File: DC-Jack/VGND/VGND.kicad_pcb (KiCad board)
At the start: 4 copper layers, 32 x 83 mm, 22 parts, among them J1 AudioJack2_Ground, J2 AudioJack2_Ground, J3 Barrel_Jack_Switch, J4 Conn_02x04_Odd_Even, J5 Conn_02x04_Odd_Even, U1 OPA1655, U2 TLE2426xLP

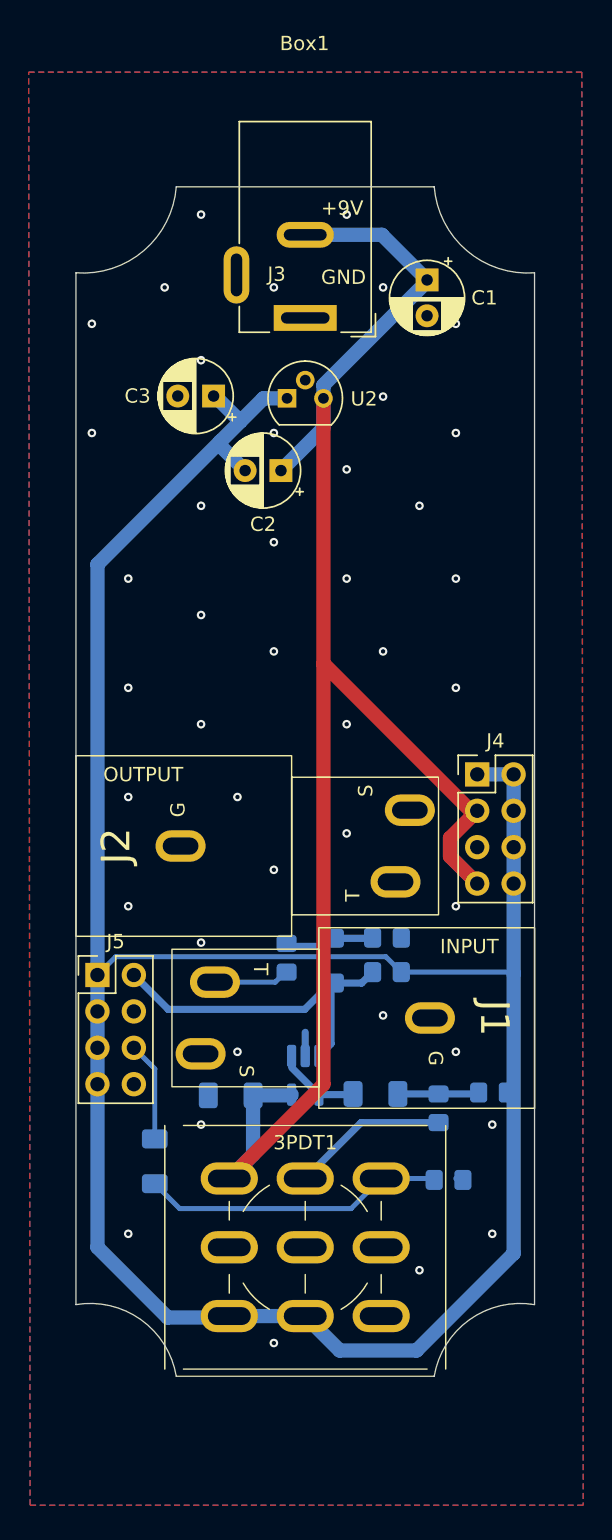
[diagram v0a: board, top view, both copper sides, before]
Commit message: Do more edge cut fixups and update for new naming
This fixes all (?) the base boards to have the symmetric outline rather
than missing one mm at the bottom.

In the process it also ends up updating the file-name information inside
the kicad files that came about due to the renames.

Off to manufacturing to see if any of them work.

Signed-off-by: Linus Torvalds <torvalds@linux-foundation.org>
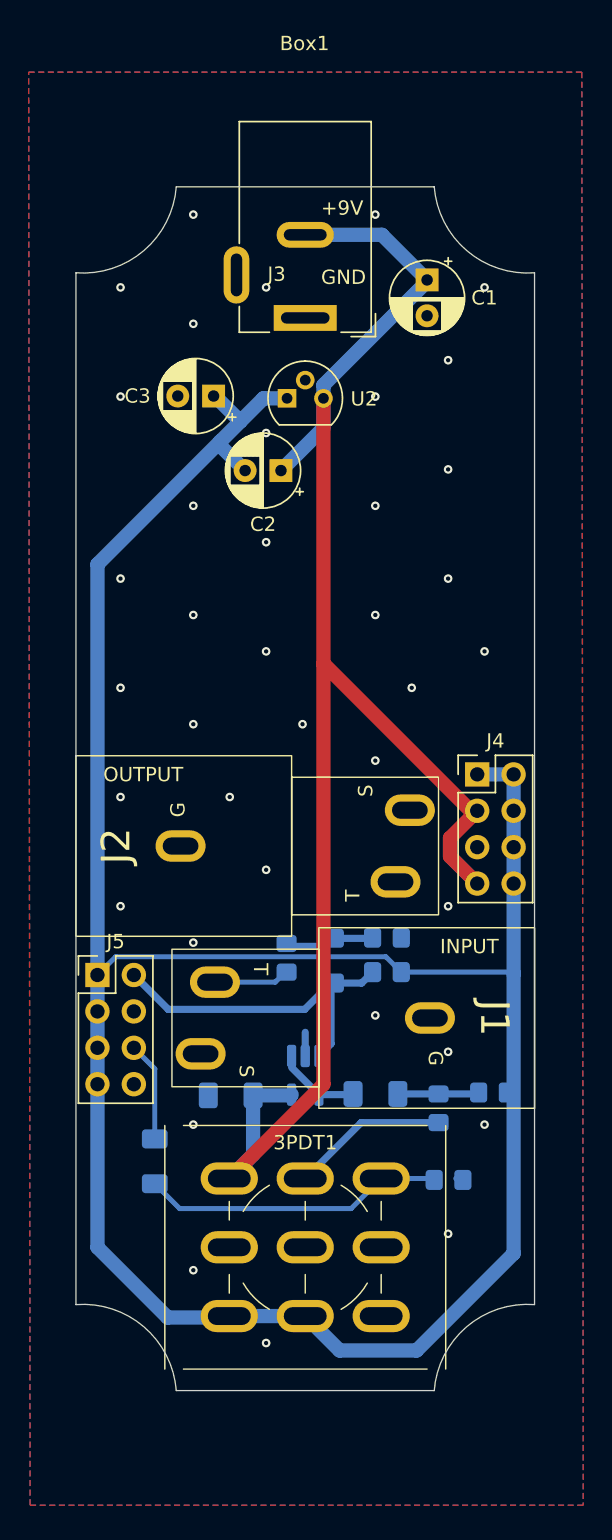
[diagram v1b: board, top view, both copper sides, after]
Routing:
- net -V: vias 42 -> 38
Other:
- board size 32 x 83 mm -> 32 x 84 mm
